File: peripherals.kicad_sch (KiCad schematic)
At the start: 2 parts

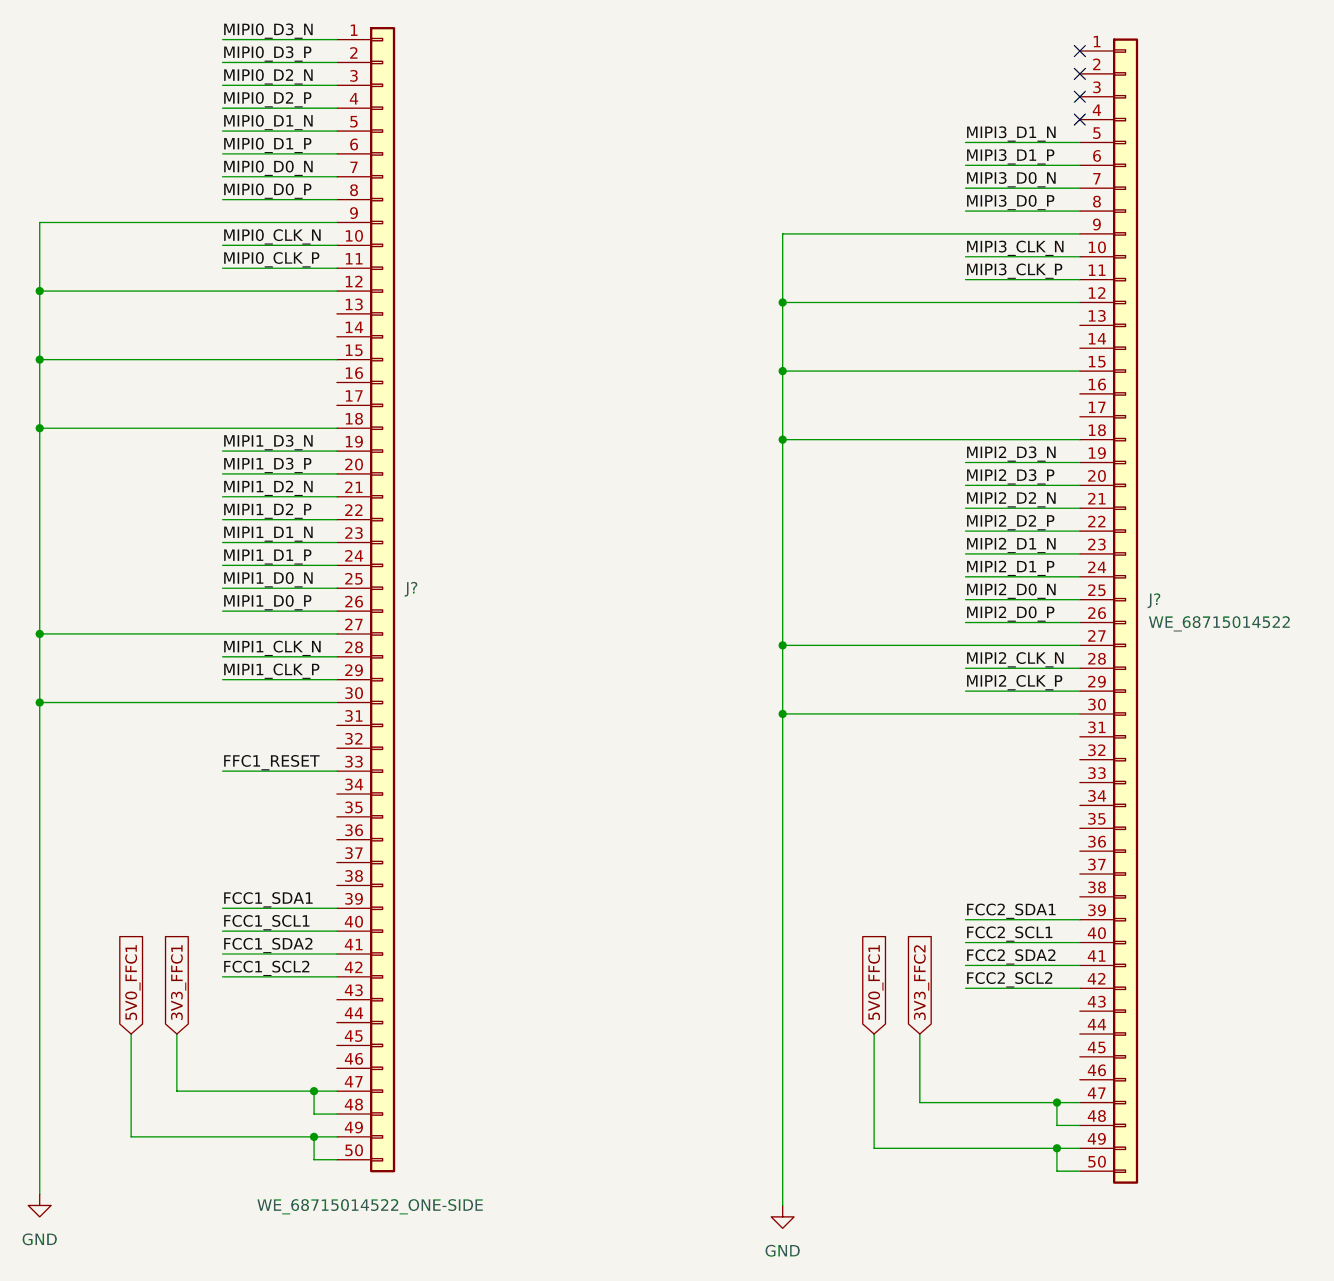
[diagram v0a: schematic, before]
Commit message: Connected soft MIPI CSI to FPGA
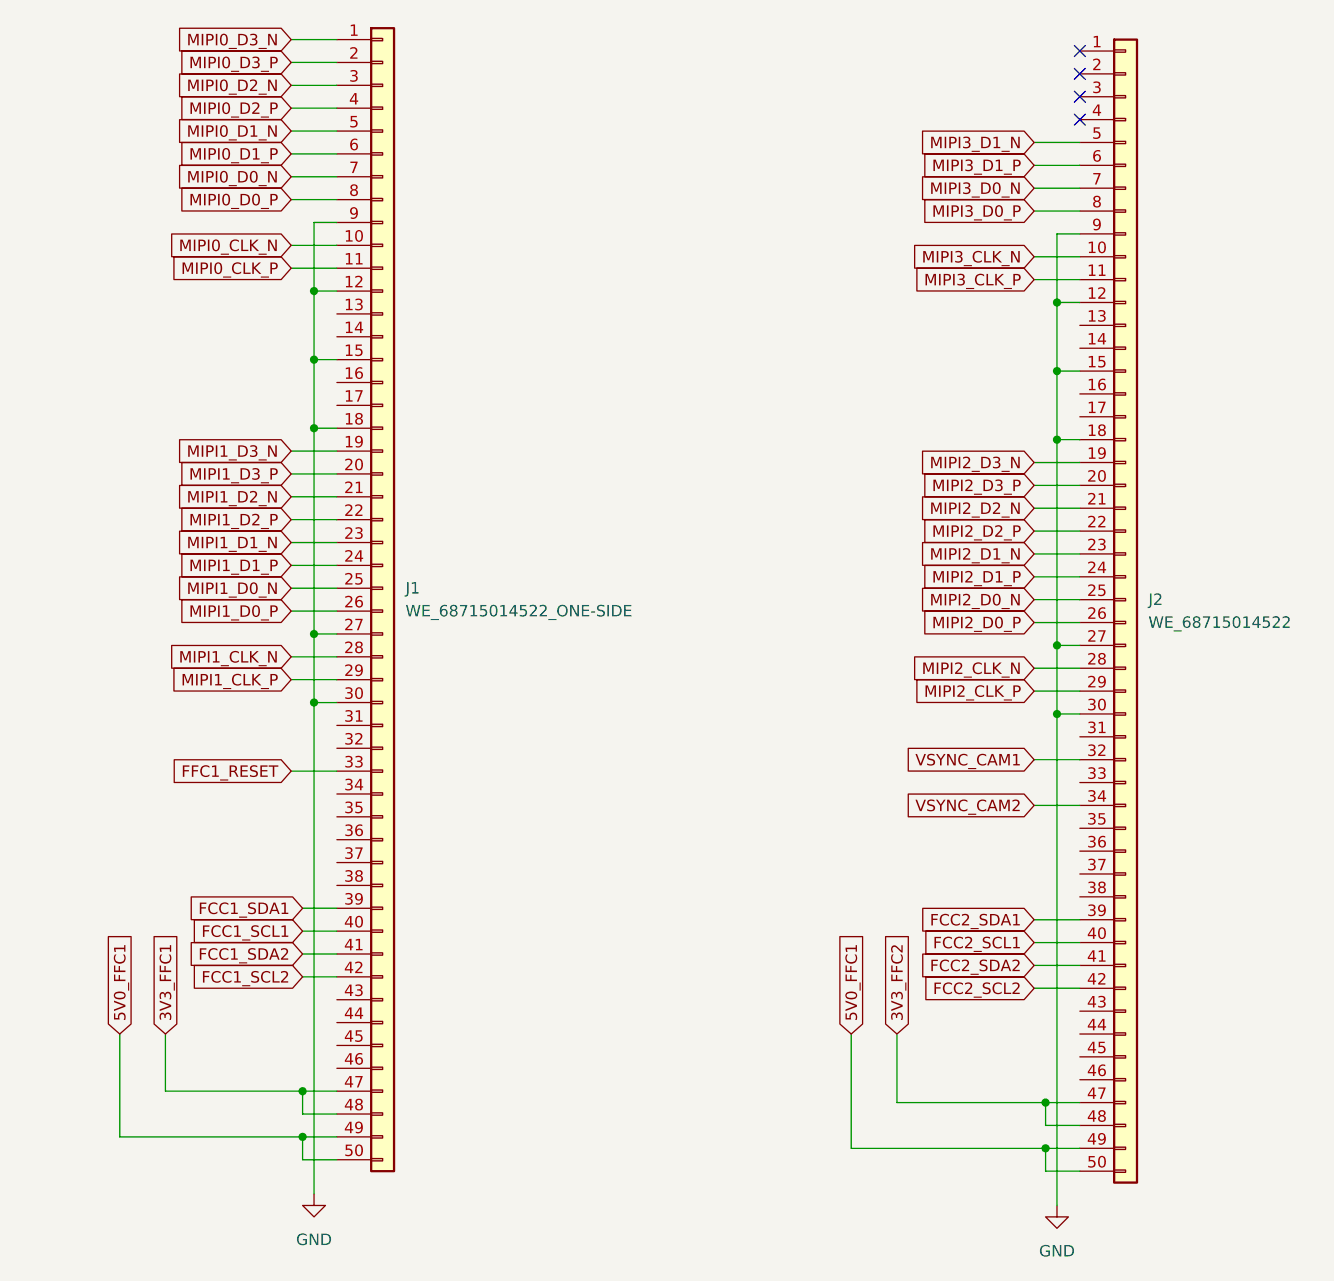
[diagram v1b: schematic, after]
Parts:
- gave numbers to parts that had none: 2
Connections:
- net VSYNC_CAM1: now reaches J2.32 (Pin_32)
- net VSYNC_CAM2: now reaches J2.34 (Pin_34)

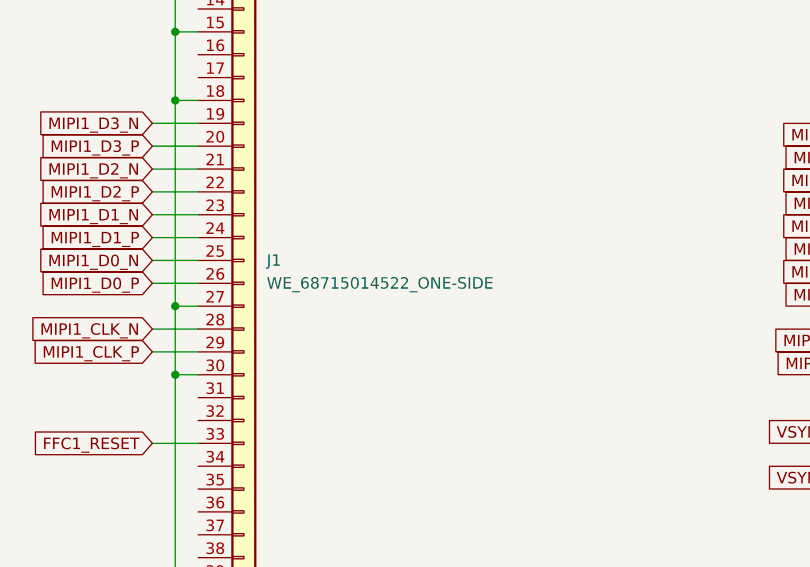
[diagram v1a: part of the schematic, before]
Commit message: Connected FPGA to power supply and added power filtering
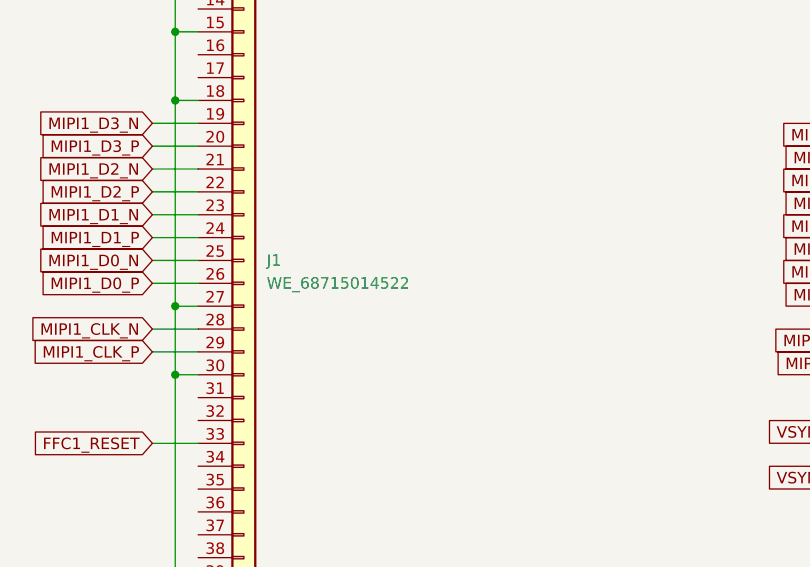
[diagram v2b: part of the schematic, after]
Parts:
- removed J1: WE_68715014522_ONE-SIDE, antmicro-footprints:WE_68715014522_ONE-SIDE, symbol antmicroFCCConnectors:WE_68715014522_ONE-SIDE
- added J1: WE_68715014522, antmicro-footprints:WE_68715014522, symbol antmicroFCCConnectors:WE_68715014522
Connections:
- net 3V3_FFC1: now also J1.47 (Pin_47), J1.48 (Pin_48)
- net 5V0_FFC1: now also J1.49 (Pin_49), J1.50 (Pin_50)
- net FCC1_SCL1: now also J1.40 (Pin_40)
- net FCC1_SCL2: now also J1.42 (Pin_42)
- net FCC1_SDA1: now also J1.39 (Pin_39)
- net FCC1_SDA2: now also J1.41 (Pin_41)
- net FFC1_RESET: now also J1.33 (Pin_33)
- net GND: now also J1.12 (Pin_12), J1.15 (Pin_15), J1.18 (Pin_18), J1.27 (Pin_27), J1.30 (Pin_30), J1.9 (Pin_9)
- net MIPI0_CLK_N: now also J1.10 (Pin_10)
- net MIPI0_CLK_P: now also J1.11 (Pin_11)
- net MIPI0_D0_N: now also J1.7 (Pin_7)
- net MIPI0_D0_P: now also J1.8 (Pin_8)
- net MIPI0_D1_N: now also J1.5 (Pin_5)
- net MIPI0_D1_P: now also J1.6 (Pin_6)
- net MIPI0_D2_N: now also J1.3 (Pin_3)
- net MIPI0_D2_P: now also J1.4 (Pin_4)
- net MIPI0_D3_N: now also J1.1 (Pin_1)
- net MIPI0_D3_P: now also J1.2 (Pin_2)
- net MIPI1_CLK_N: now also J1.28 (Pin_28)
- net MIPI1_CLK_P: now also J1.29 (Pin_29)
- net MIPI1_D0_N: now also J1.25 (Pin_25)
- net MIPI1_D0_P: now also J1.26 (Pin_26)
- net MIPI1_D1_N: now also J1.23 (Pin_23)
- net MIPI1_D1_P: now also J1.24 (Pin_24)
- net MIPI1_D2_N: now also J1.21 (Pin_21)
- net MIPI1_D2_P: now also J1.22 (Pin_22)
- net MIPI1_D3_N: now also J1.19 (Pin_19)
- net MIPI1_D3_P: now also J1.20 (Pin_20)
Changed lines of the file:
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@@
     )
   )
-  (symbol (lib_id "antmicroFCCConnectors:WE_68715014522_ONE-SIDE") (at 90.17 67.31 0) (unit 1)
-    (in_bom yes) (on_board yes)
-    (property "Reference" "J1" (id 0) (at 92.71 87.6299 0)
+  (symbol (lib_id "power:GND") (at 165.1 156.21 0) (unit 1)
+    (in_bom yes) (on_board yes) (fields_autoplaced)
+    (property "Reference" "#PWR0178" (id 0) (at 165.1 162.56 0)
+      (effects (font (size 1.27 1.27)) hide)
+    )
+    (property "Value" "GND" (id 1) (at 165.1 161.29 0))
+    (property "Footprint" "" (id 2) (at 165.1 156.21 0)
+      (effects (font (size 1.27 1.27)) hide)
+    )
+    (property "Datasheet" "" (id 3) (at 165.1 156.21 0)
+      (effects (font (size 1.27 1.27)) hide)
+    )
+    (pin "1")
+  )
+  (symbol (lib_id "power:GND") (at 82.55 154.94 0) (unit 1)
+    (in_bom yes) (on_board yes) (fields_autoplaced)
+    (property "Reference" "#PWR0177" (id 0) (at 82.55 161.29 0)
+      (effects (font (size 1.27 1.27)) hide)
+    )
+    (property "Value" "GND" (id 1) (at 82.55 160.02 0))
+    (property "Footprint" "" (id 2) (at 82.55 154.94 0)
+      (effects (font (size 1.27 1.27)) hide)
+    )
+    (property "Datasheet" "" (id 3) (at 82.55 154.94 0)
+      (effects (font (size 1.27 1.27)) hide)
+    )
+    (pin "1")
+  )
+  (symbol (lib_id "antmicroFCCConnectors:WE_68715014522") (at 172.72 68.58 0) (unit 1)
+    (in_bom yes) (on_board yes) (fields_autoplaced)
+    (property "Reference" "J2" (id 0) (at 175.26 88.8999 0)
       (effects (font (size 1.27 1.27)) (justify left))
     )
-    (property "Value" "WE_68715014522_ONE-SIDE" (id 1) (at 92.71 90.17 0)
+    (property "Value" "WE_68715014522" (id 1) (at 175.26 91.4399 0)
       (effects (font (size 1.27 1.27)) (justify left))
     )
-    (property "Footprint" "antmicro-footprints:WE_68715014522_ONE-SIDE" (id 2) (at 85.09 157.48 0)
+    (property "Footprint" "antmicro-footprints:WE_68715014522" (id 2) (at 167.64 158.75 0)
       (effects (font (size 1.27 1.27)) hide)
     )
-    (property "Datasheet" "" (id 3) (at 90.17 160.02 0)
+    (property "Datasheet" "https://katalog.we-online.de/em/datasheet/6871xx14522.pdf" (id 3) (at 172.72 161.29 0)
       (effects (font (size 1.27 1.27)) hide)
     )
-    (property "MPN" "68715014522 " (id 4) (at 100.33 82.55 0)
+    (property "MPN" "68715014522 " (id 4) (at 182.88 83.82 0)
       (effects (font (size 1.524 1.524)) (justify left) hide)
     )
-    (property "Manufacturer" "Wurth Elektronik " (id 5) (at 106.68 113.03 0)
+    (property "Manufacturer" "Wurth Elektronik " (id 5) (at 189.23 114.3 0)
       (effects (font (size 1.524 1.524)) (justify left) hide)
     )
@@
     (pin "9")
   )
-  (symbol (lib_id "power:GND") (at 165.1 156.21 0) (unit 1)
+  (symbol (lib_id "antmicroFCCConnectors:WE_68715014522") (at 90.17 67.31 0) (unit 1)
     (in_bom yes) (on_board yes) (fields_autoplaced)
-    (property "Reference" "#PWR0178" (id 0) (at 165.1 162.56 0)
+    (property "Reference" "J1" (id 0) (at 92.71 87.6299 0)
+      (effects (font (size 1.27 1.27)) (justify left))
+    )
+    (property "Value" "WE_68715014522" (id 1) (at 92.71 90.1699 0)
+      (effects (font (size 1.27 1.27)) (justify left))
+    )
+    (property "Footprint" "antmicro-footprints:WE_68715014522" (id 2) (at 85.09 157.48 0)
       (effects (font (size 1.27 1.27)) hide)
     )
-    (property "Value" "GND" (id 1) (at 165.1 161.29 0))
-    (property "Footprint" "" (id 2) (at 165.1 156.21 0)
+    (property "Datasheet" "https://katalog.we-online.de/em/datasheet/6871xx14522.pdf" (id 3) (at 90.17 160.02 0)
       (effects (font (size 1.27 1.27)) hide)
     )
-    (property "Datasheet" "" (id 3) (at 165.1 156.21 0)
-      (effects (font (size 1.27 1.27)) hide)
-    )
-    (pin "1")
-  )
-  (symbol (lib_id "power:GND") (at 82.55 154.94 0) (unit 1)
-    (in_bom yes) (on_board yes) (fields_autoplaced)
-    (property "Reference" "#PWR0177" (id 0) (at 82.55 161.29 0)
-      (effects (font (size 1.27 1.27)) hide)
-    )
-    (property "Value" "GND" (id 1) (at 82.55 160.02 0))
-    (property "Footprint" "" (id 2) (at 82.55 154.94 0)
-      (effects (font (size 1.27 1.27)) hide)
-    )
-    (property "Datasheet" "" (id 3) (at 82.55 154.94 0)
-      (effects (font (size 1.27 1.27)) hide)
-    )
-    (pin "1")
-  )
-  (symbol (lib_id "antmicroFCCConnectors:WE_68715014522") (at 172.72 68.58 0) (unit 1)
-    (in_bom yes) (on_board yes) (fields_autoplaced)
-    (property "Reference" "J2" (id 0) (at 175.26 88.8999 0)
-      (effects (font (size 1.27 1.27)) (justify left))
-    )
-    (property "Value" "WE_68715014522" (id 1) (at 175.26 91.4399 0)
-      (effects (font (size 1.27 1.27)) (justify left))
-    )
-    (property "Footprint" "antmicro-footprints:WE_68715014522" (id 2) (at 167.64 158.75 0)
-      (effects (font (size 1.27 1.27)) hide)
-    )
-    (property "Datasheet" "https://katalog.we-online.de/em/datasheet/6871xx14522.pdf" (id 3) (at 172.72 161.29 0)
-      (effects (font (size 1.27 1.27)) hide)
-    )
-    (property "MPN" "68715014522 " (id 4) (at 182.88 83.82 0)
+    (property "MPN" "68715014522 " (id 4) (at 100.33 82.55 0)
       (effects (font (size 1.524 1.524)) (justify left) hide)
     )
-    (property "Manufacturer" "Wurth Elektronik " (id 5) (at 189.23 114.3 0)
+    (property "Manufacturer" "Wurth Elektronik " (id 5) (at 106.68 113.03 0)
       (effects (font (size 1.524 1.524)) (justify left) hide)
     )

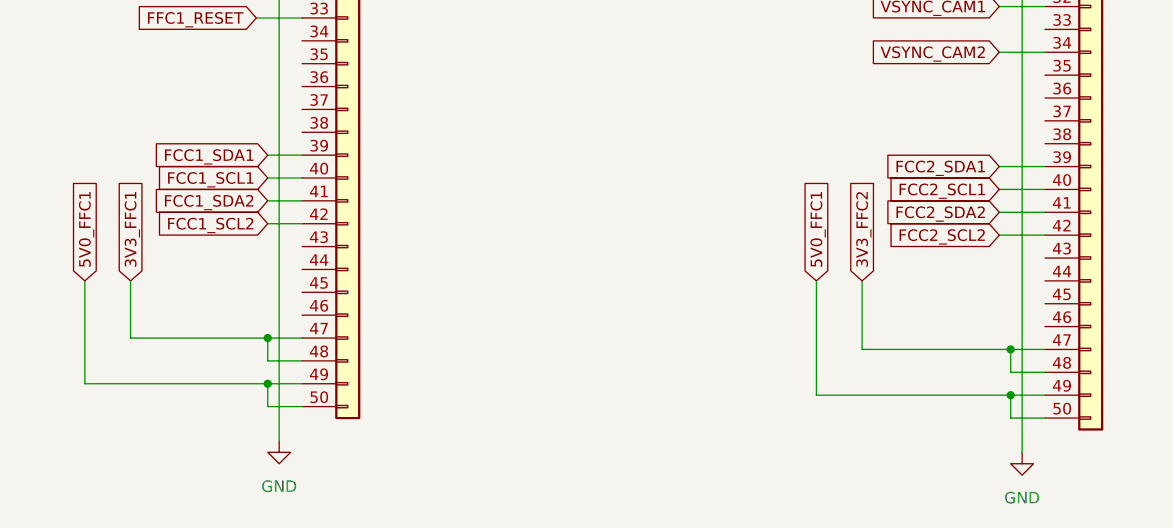
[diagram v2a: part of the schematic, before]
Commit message: Added power testpoints
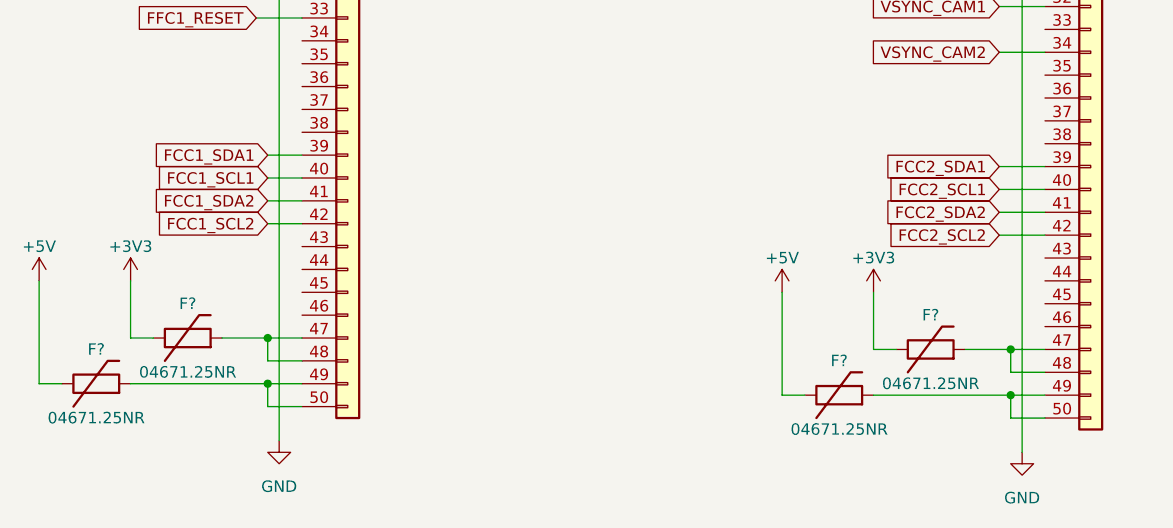
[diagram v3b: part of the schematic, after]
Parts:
- added F? (x4): 04671.25NR, antmicro-footprints:0603-Fuse-Littelfuse-0467, symbol antmicroFuses:04671.25NR
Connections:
- net 3V3_FFC1: no longer names the net of J1.47 (Pin_47), J1.48 (Pin_48)
- net 3V3_FFC1: now also F?.2
- net 3V3_FFC2: no longer names the net of J2.47 (Pin_47), J2.48 (Pin_48)
- net 3V3_FFC2: now also F?.2
- net 5V0_FFC1: no longer names the net of J2.49 (Pin_49), J2.50 (Pin_50)
- net 5V0_FFC1: now also F?.2; no longer J1.49 (Pin_49), J1.50 (Pin_50)
- new net: F?.2, J1.49 (Pin_49), J1.50 (Pin_50)
- new net +3V3: F?.1, F?.1
- new net +5V: F?.1, F?.1
